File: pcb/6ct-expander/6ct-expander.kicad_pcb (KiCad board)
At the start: 2 copper layers, 88 x 30 mm, 57 parts, among them J1 SJ-3524-SMT-TR, J2 SJ-3524-SMT-TR, J3 SJ-3524-SMT-TR, J4 SJ-3524-SMT-TR, J5 SJ-3524-SMT-TR, J6 SJ-3524-SMT-TR, J7 Conn_02x05_Odd_Even

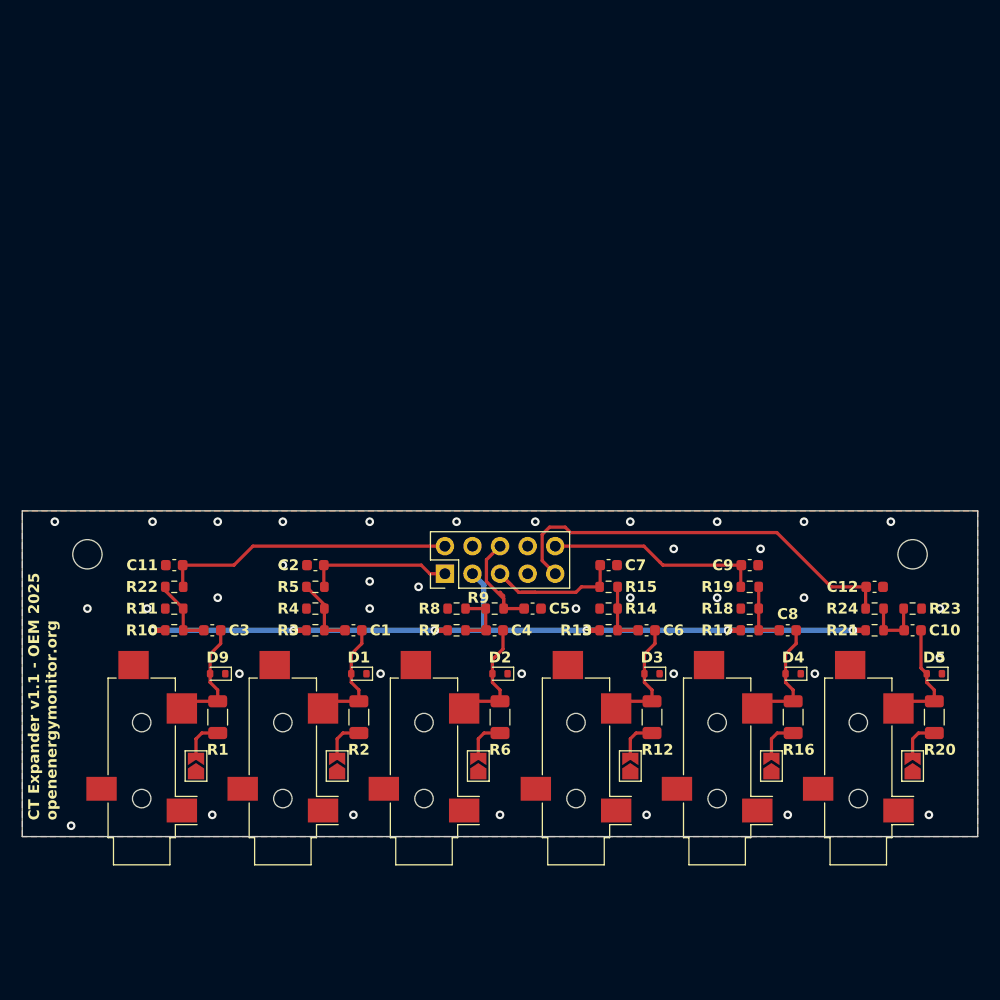
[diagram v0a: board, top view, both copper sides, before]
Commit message: [6CT] Correct header, add extra GND pads
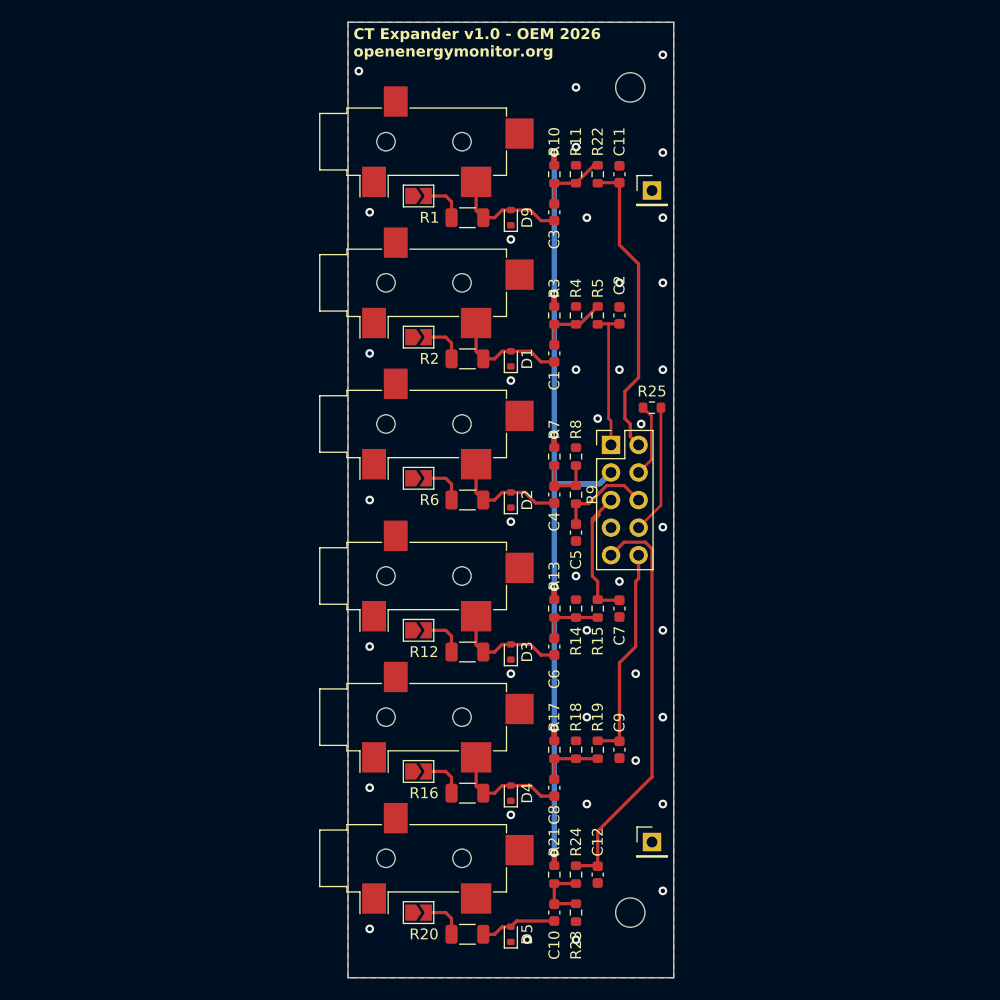
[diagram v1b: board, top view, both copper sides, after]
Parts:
- added J8: Conn_01x01, Connector_PinHeader_2.54mm:PinHeader_1x01_P2.54mm_Vertical, F.Cu at (158.0, 130.5)
- added J9: Conn_01x01, Connector_PinHeader_2.54mm:PinHeader_1x01_P2.54mm_Vertical, F.Cu at (158.0, 70.5)
- added R25: 47K, Resistor_SMD:R_0603_1608Metric, F.Cu at (158.0, 90.5)
- moved H1 65.9 mm to (156.0, 61.0), turned to 0 degrees
- moved J1 63.2 mm to (136.0, 66.0), turned to 90 degrees
- moved JP1 56.4 mm to (136.5, 71.0), turned to 0 degrees
- moved R10 54.7 mm to (149.0, 69.0), turned to -90 degrees
- moved C11 54.6 mm to (155.0, 69.0), turned to 90 degrees
- moved R11 54.5 mm to (151.0, 69.0), turned to -90 degrees
- moved R22 54.5 mm to (153.0, 69.0), turned to 90 degrees
- moved R1 51.4 mm to (141.0, 73.0), turned to 180 degrees
- moved D9 49.9 mm to (145.0, 73.0), turned to 90 degrees
- moved C3 49.7 mm to (149.0, 72.5), turned to 90 degrees
- moved JP6 47.5 mm to (136.5, 137.0), turned to 0 degrees
- moved R20 47.4 mm to (141.0, 139.0), turned to 180 degrees
- moved J2 46.6 mm to (136.0, 79.0), turned to 90 degrees
- moved D5 45.8 mm to (145.0, 139.0), turned to 90 degrees
- moved C10 42.0 mm to (149.0, 137.0), turned to 90 degrees
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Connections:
- J7 pad 4: GND -> /SENSE
- J7 pad 8: unconnected-(J7-Pin_8-Pad8) -> +3V3
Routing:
- net +3V3: track 0.00 -> 11.9 mm
- net /SENSE: track 0.00 -> 6.77 mm
- net Net-(D5-A2): track 10.6 -> 7.04 mm
- net /V_{REF}: track 77.2 -> 79.2 mm
- net /CT10: track 14.8 -> 13.0 mm
- net /CT9: track 10.5 -> 9.38 mm
- net /CT7: track 26.8 -> 27.9 mm
- net /CT12: track 38.5 -> 37.8 mm
- net GND: vias 38 -> 39
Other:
- board size 88 x 30 mm -> 30 x 88 mm
- board text added: "CT Expander v1.0 - OEM 2026 openenergymonitor.org"
- board text removed: "CT Expander v1.1 - OEM 2025 openenergymonitor.org"
